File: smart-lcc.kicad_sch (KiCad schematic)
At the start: 83 parts, among them J1 280372-1, J2 F0503-ZV-24-20T-R, J3 Conn_01x24, J4 BM04B-SRSS-TB(LF)(SN), J5 BM04B-SRSS-TB(LF)(SN), J6 Micro_SD_Card_Det2, Q1 2N7002, Q2 2N7002, Q3 2N7002, SW1 SW_Push, SW2 SW_Push, U1 MAX40200AUK, U2 RP2040, U3 ESP32-S3-WROOM-1, U4 W25Q16JVSNIQ (Program Flash), U5 W25Q16JVSNIQ (Opt. Settings f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, U6 MAX40200AUK, U7 74LVC1G125, U8 LM5050-1, Y1 XYDBPCNANF-12MHZ

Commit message: R2A WIP
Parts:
- removed Q3: 2N7002, Package_TO_SOT_SMD:SOT-23, symbol Transistor_FET:2N7002
- removed TP11, TP12, TP13, TP14, TP15, TP16: TestPoint_Small, TestPoint:TestPoint_Pad_D1.0mm, symbol Connector:TestPoint_Small
- removed U1, U6: MAX40200AUK, Package_TO_SOT_SMD:SOT-23-5, symbol Analog_Switch:MAX40200AUK
- removed U8: LM5050-1, Package_TO_SOT_SMD:TSOT-23-6, symbol Power_Management:LM5050-1
- added C25, C27: 22 uF, 10V, X7T, Capacitor_SMD:C_0805_2012Metric, symbol Device:C_Small
- added C26: 5.6 nF, 50V, C0G, Capacitor_SMD:C_0402_1005Metric, symbol Device:C_Small
- added C33: 10 μF, 25 V, X7R, Capacitor_SMD:C_1206_3216Metric, symbol Device:C_Small
- added D4, D5: 19-217/BHC-ZL1M2RY/3T, LED_SMD:LED_0603_1608Metric, symbol Device:LED
- added D6, D7: D_Schottky, Diode_SMD:D_SOD-128, symbol Device:D_Schottky
- added J7: Conn_01x12, TFT_1.47IN_172X320_12P:TFT_1.47IN_172X320_12P, symbol Connector_Generic:Conn_01x12
- added J8: BM04B-SRSS-TB(LF)(SN), BM04B-SRSS-TB_LF__SN_:JST_BM04B-SRSS-TB(LF)(SN), symbol BM04B-SRSS-TB_LF__SN_:BM04B-SRSS-TB(LF)(SN)
- added JP2: SolderJumper_3_Bridged12, Jumper:SolderJumper-3_P1.3mm_Bridged2Bar12_RoundedPad1.0x1.5mm, symbol Jumper:SolderJumper_3_Bridged12
- added Q4: 2N7002, Package_TO_SOT_SMD:SOT-23, symbol Transistor_FET:2N7002
- added R12, R23: 100R, Resistor_SMD:R_0402_1005Metric, symbol Device:R_Small
- added R13, R15, R16, R17, R24, R25: 4K7, Resistor_SMD:R_0402_1005Metric, symbol Device:R
- added R18: 10R, Resistor_SMD:R_0402_1005Metric, symbol Device:R_Small
- added R19, R21, R22: 10K, Resistor_SMD:R_0402_1005Metric, symbol Device:R_Small
- added R20: 31K6, Resistor_SMD:R_0402_1005Metric, symbol Device:R_Small
- added TP13: TestPoint, TestPoint:TestPoint_Pad_D1.0mm, symbol Connector:TestPoint
- added TP14, TP15, TP16, TP19: TestPoint, TestPoint:TestPoint_Pad_D1.5mm, symbol Connector:TestPoint
- added TP20, TP21, TP22, TP23, TP24, TP25, TP26, TP27: TestPoint_Small, TestPoint:TestPoint_Pad_D1.5mm, symbol Connector:TestPoint_Small
- added TP28, TP29: TestPoint_Small, TestPoint:TestPoint_Pad_D1.0mm, symbol Connector:TestPoint_Small
- added U6: TPS82130, Package_LGA:Texas_SIL0008D_MicroSiP-8-1EP_2.8x3mm_P0.65mm_EP1.1x1.9mm_ThermalVias, symbol Regulator_Switching:TPS82130
- C10, C13, C14, C15, C16, C17, C18, C19, C20, C21, C22, C24, C9: value 100 nF -> 100 nF, 50V, X7R
- C28: value 22uF, 10V, X5R -> 22 uF, 10V, X5R; footprint Capacitor_SMD:C_0805_2012Metric -> Capacitor_SMD:C_0603_1608Metric; LCSC C2177954 -> C2980159
- C5, C6: now not fitted; now left out of the parts list
- J1, JP1, SW1, TP1, TP10, TP17, TP18, TP2, TP3, TP4, TP5, TP6, TP7, TP8, TP9: now left out of the parts list
- R14, R7: LCSC C3017451 -> C4288031
- R2, R3: value 20R -> 100R; JLCPCB Basic N -> (none); LCSC C2909334 -> C2935235
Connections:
- net +3V3: now also C4.1, J3.5 (Pin_5), J7.4 (Pin_4), J8.2, JP2.2 (C), R13.2, R15.2, R16.2, R17.2, R18.1, R24.2, R25.2, TP26.1
- net 12V_OLED: now also D7.2 (A)
- net 3V3_MCU: now also JP2.3 (B)
- net ESP32_USB_DN: now also TP28.1
- net ESP32_USB_DP: now also TP29.1
- net GND: now also C25.2, C26.2, C27.2, C33.1, D4.1 (K), D5.1 (K), J7.1 (Pin_1), J7.12 (Pin_12), J7.5 (Pin_5), J7.6 (Pin_6), J8.1, J8.S1 (SHIELD), J8.S2 (SHIELD), Q4.2 (S), R19.1, R21.2, R22.2, TP20.1, U6.3 (GND), U6.9 (GND)
- net RP2040_QWIIC1_SCL: now also R16.1
- net RP2040_QWIIC1_SDA: now also R17.1
- net RP2040_QWIIC2_SCL: now also R13.1
- net RP2040_QWIIC2_SDA: now also R15.1
- net RP2040_SD_DET_A: now also U2.18 (GPIO15); no longer U2.17 (GPIO14)
- net RP2040_SD_DET_B: now also U2.27 (GPIO16); no longer U2.18 (GPIO15)
- net RP2040_SERIAL_BOOT: now also U2.36 (GPIO24); no longer U2.27 (GPIO16)
- net RP2040_SET_CS: now also U2.28 (GPIO17); no longer U2.16 (GPIO13)
- net RX_FROM_CONTROL_BOARD_5V: now also R21.1
- net SSD1309_CS: now also J7.8 (Pin_8), TP24.1
- net SSD1309_DC: now also J7.7 (Pin_7), TP25.1
- net SSD1309_MOSI: now also J7.10 (Pin_10), TP22.1
- net SSD1309_RES: now also J7.11 (Pin_11), TP21.1
- net SSD1309_SCLK: now also J7.9 (Pin_9), TP23.1
- net SW_MINUS: now also SW2.2, U3.23 (GPIO21); no longer SW1.2, U3.31 (GPIO38/FSPIWP/SUBSPIWP)
- net SW_PLUS: now also SW1.2, U3.31 (GPIO38/FSPIWP/SUBSPIWP); no longer SW2.2, U3.23 (GPIO21)
- net TX_TO_CONTROL_BOARD: now also R22.1
- net at U2.37 (GPIO25): now also R23.1
- net at U2.38 (GPIO26_ADC0): now also TP14.1
- net at U2.39 (GPIO27_ADC1): now also TP15.1
- net at U2.40 (GPIO28_ADC2): now also TP16.1
- net at U2.41 (GPIO29_ADC3): now also TP19.1
- net BACKLIGHT: now reaches U3.24 (GPIO47/SPICLK_P/SUBSPICLK_P_DIFF)
- net BACKLIGHT: now also Q4.1 (G), TP27.1
- net at U3.25 (GPIO48/SPICLK_N/SUBSPICLK_N_DIFF): now also R12.1
- net ESP32_QWIIC_SDA: now reaches U3.38 (GPIO2/TOUCH2/ADC1_CH1)
- net ESP32_QWIIC_SDA: now also J8.3, R24.1
- net ESP32_QWIIC_SCL: now reaches U3.39 (GPIO1/TOUCH1/ADC1_CH0)
- net ESP32_QWIIC_SCL: now also J8.4, R25.1
- net at U3.7 (GPIO7/TOUCH7/ADC1_CH6): now also TP13.1
- net RP2040_SET_D3: now reaches U5.3 (~{WP}/IO2)
- net RP2040_SET_D3: now also U2.17 (GPIO14)
- net RP2040_SET_D2: now reaches U5.7 (~{HOLD}/IO3)
- net RP2040_SET_D2: now also U2.16 (GPIO13)
- net 12V_OLED_SAFE: no longer names the net of J2.3 (Pin_3), J2.4 (Pin_4)
- net 12V_OLED_SAFE: now also D6.2 (A); no longer C1.1, J3.23 (Pin_23)
- removed net 3V3_OLED_SAFE: C4.1, J2.6 (Pin_6), J3.5 (Pin_5)
- new net: J7.2 (Pin_2), Q4.3 (D)
- new net: C26.1, U6.8 (SS/TR)
- new net: D5.2 (A), R23.2
- new net: J7.3 (Pin_3), R18.2
- new net: R19.2, R20.2, U6.6 (FB)
- new net: D4.2 (A), R12.2
- new net 3V3_OUT: C25.1, C27.1, JP2.1 (A), R20.1, U6.4 (VOUT), U6.5 (VOUT)
- new net VIN: C1.1, C33.2, D6.1 (K), D7.1 (K), J3.23 (Pin_23), U6.1 (EN), U6.2 (VIN)
- no-connect marks 20 -> 7
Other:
- note added: "DC-DC converter (12V -> 3.3V)"
- note added: "ST7789V connector"
- moved on the sheet: D3, J4, J5, JP1, R4, TP10, TP17, TP18, TP9

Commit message: Initial work on R2B
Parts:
- removed D6, D7: D_Schottky, Diode_SMD:D_SOD-128, symbol Device:D_Schottky
- added Q3, Q5: 2N7002, Package_TO_SOT_SMD:SOT-23, symbol PCM_Transistor_MOSFET_AKL:2N7002
- added U1, U8: LM5050-1, Package_TO_SOT_SMD:TSOT-23-6, symbol Power_Management:LM5050-1
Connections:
- net 12V_OLED: now also Q5.2 (S), U1.4 (IN)
- net GND: now also U1.2 (GND), U8.2 (GND)
- net VIN: now also Q3.3 (D), Q5.3 (D), U1.1 (VS), U1.6 (OUT), U8.1 (VS), U8.6 (OUT)
- net VIN_DEBUG: now reaches J2.3 (Pin_3), J2.4 (Pin_4)
- net VIN_DEBUG: now also Q3.2 (S), U8.4 (IN)
- new net: Q3.1 (G), U8.5 (GATE)
- new net: Q5.1 (G), U1.5 (GATE)
- no-connect marks 7 -> 9

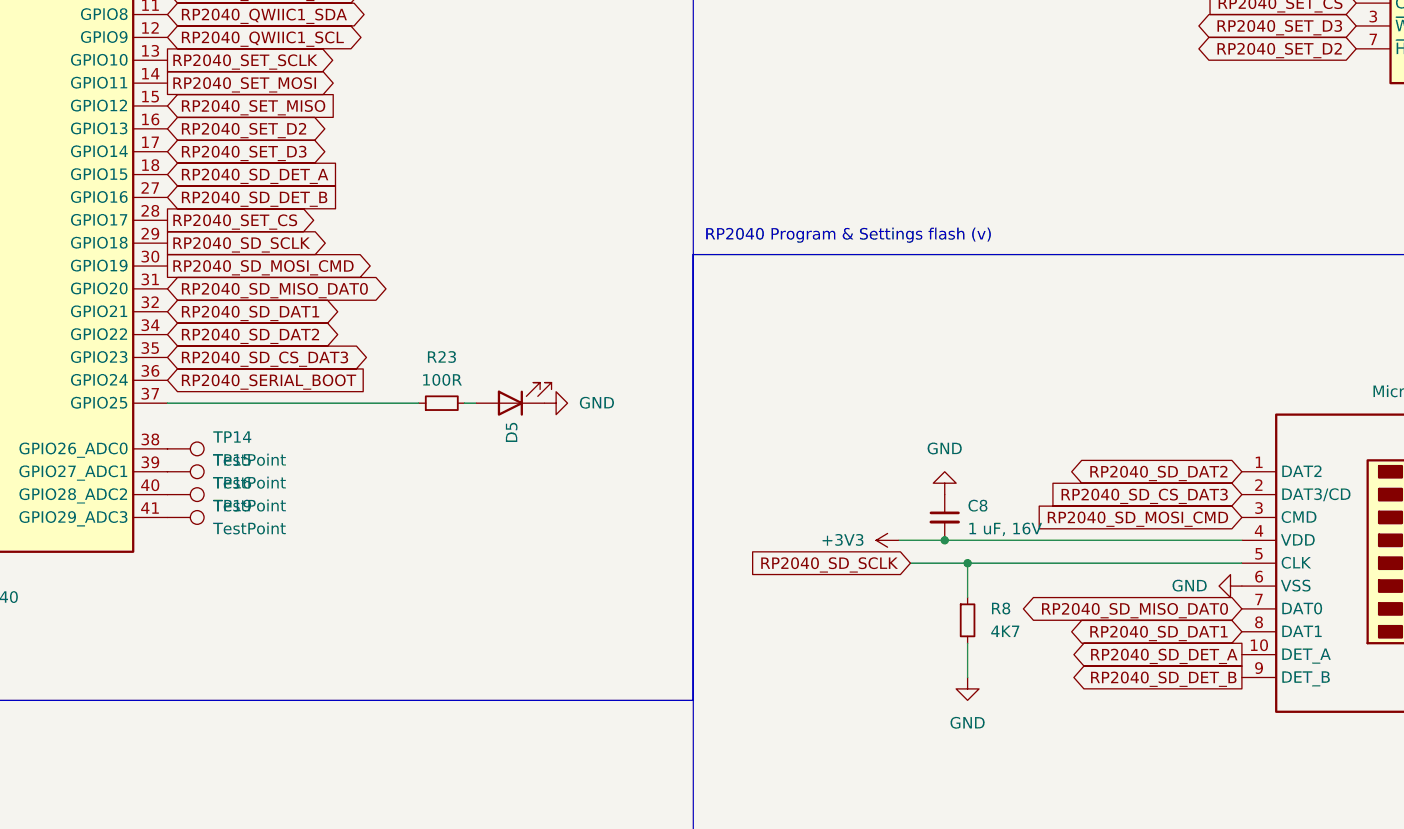
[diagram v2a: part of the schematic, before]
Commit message: Removed SD_DET_A from RP2040 and connected DET_A on the SD card to GND
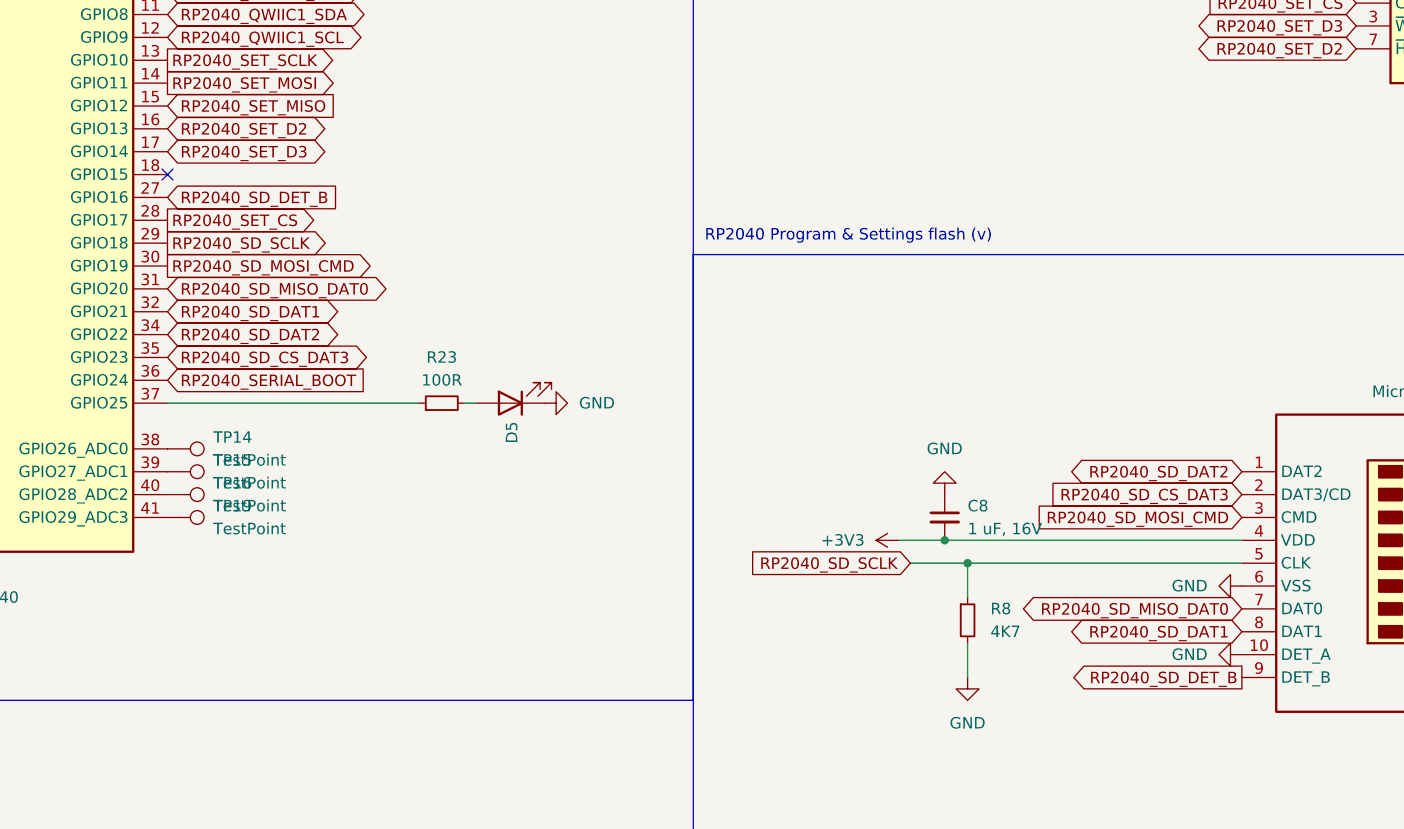
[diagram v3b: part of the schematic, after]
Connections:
- net GND: now also J6.10 (DET_A)
- net RP2040_SD_DET_A: no longer names the net of U2.18 (GPIO15)
- net RP2040_SD_DET_A: no longer J6.10 (DET_A)
- no-connect marks 9 -> 10
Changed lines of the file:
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@@
   (no_connect (at 25.4 149.86))
   (no_connect (at 255.27 326.39))
+  (no_connect (at 373.38 153.67))
   (no_connect (at 69.85 316.23))
   (no_connect (at 134.62 44.45))
@@
     )
   )
-  (global_label "RP2040_SD_DET_A" (shape output) (at 492.76 207.01 180) (fields_autoplaced)
-    (effects (font (size 1.27 1.27)) (justify right))
-    (property "Intersheetrefs" "${INTERSHEET_REFS}" (at 473.1935 207.01 0)
-      (effects (font (size 1.27 1.27)) (justify right) hide)
-    )
-  )
   (global_label "ESP32_EN" (shape input) (at 227.33 260.35 180) (fields_autoplaced)
     (effects (font (size 1.27 1.27)) (justify right))
@@
     )
   )
-  (global_label "RP2040_SD_DET_A" (shape input) (at 373.38 153.67 0) (fields_autoplaced)
-    (effects (font (size 1.27 1.27)) (justify left))
-    (property "Intersheetrefs" "${INTERSHEET_REFS}" (at 392.9465 153.67 0)
-      (effects (font (size 1.27 1.27)) (justify left) hide)
-    )
-  )
   (global_label "RP2040_SET_D2" (shape bidirectional) (at 505.46 139.7 180) (fields_autoplaced)
     (effects (font (size 1.27 1.27)) (justify right))
@@
         )
       )
+    )
+  )
+  (symbol (lib_id "power:GND") (at 492.76 207.01 270) (unit 1)
+    (in_bom yes) (on_board yes) (dnp no) (fields_autoplaced)
+    (property "Reference" "#PWR090" (at 486.41 207.01 0)
+      (effects (font (size 1.27 1.27)) hide)
+    )
+    (property "Value" "GND" (at 488.95 207.01 90)
+      (effects (font (size 1.27 1.27)) (justify right))
+    )
+    (property "Footprint" "" (at 492.76 207.01 0)
+      (effects (font (size 1.27 1.27)) hide)
+    )
+    (property "Datasheet" "" (at 492.76 207.01 0)
+      (effects (font (size 1.27 1.27)) hide)
+    )
+    (pin "1")
+    (instances
+      (project "smart-lcc"
+        (path "/8090f672-69d7-45b0-9be9-e805048b83ac"
+          (reference "#PWR090") (unit 1)
+        )
+      )
